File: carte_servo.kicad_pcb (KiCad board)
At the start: 4 copper layers, 48.4 x 99.2 mm, 157 parts, among them J1 Conn_01x04_Pin, J10 Conn_01x03_Male, J11 Transistor_2, J12 Transistor_1, J13 Transistor_4, J14 Transistor_.3, J16 Conn_01x04_Male, J17 Conn_01x04_Male, J18 Conn_01x03_Male, J19 Conn_01x03_Male, J2 Conn_02x04_Top_Bottom, J24 Conn_LEDs, J25 Conn_AX12, J29 Conn_AX12, J3 Conn_01x04_Pin, J5 Conn_01x03_Male, J6 Conn_01x03_Male, J7 Conn_01x03_Male, J8 Conn_01x03_Male, J9 Conn_01x03_Male, P1 USB_C_Plug_USB2.0, Q1 DMN2011UTS, Q2 DMN2011UTS, Q3 DMN2011UTS, Q4 DMN2011UTS, Q6 DMN2011UTS, Q7 CSD17307Q5A, Q8 CSD17579Q5A, SW2 SW_Push, U1 XGZP6897D_differential_pressu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, U10 TPS563200, U2 XGZP6897D_differential_pressu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, U3 TMC2208_SILENTSTEPSTICK, U4 TMC2208_SILENTSTEPSTICK, U5 74LVC2G241, U6 SN65HVD230, U7 LD1117S33TR_SOT223, U8 ESP32-S3-WROOM-1, U9 LM3150MH

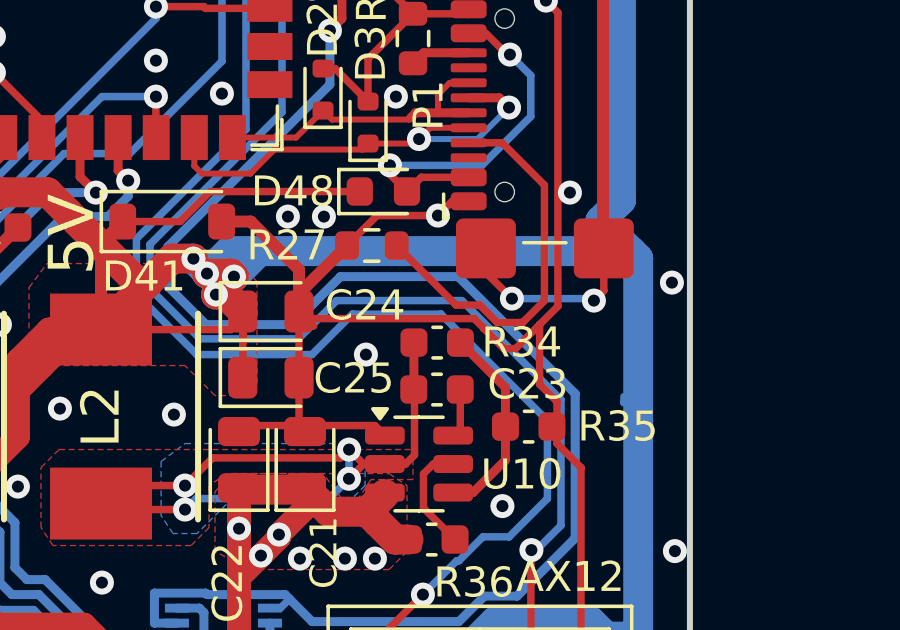
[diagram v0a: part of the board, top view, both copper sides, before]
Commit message: fix DCDC5V schematic
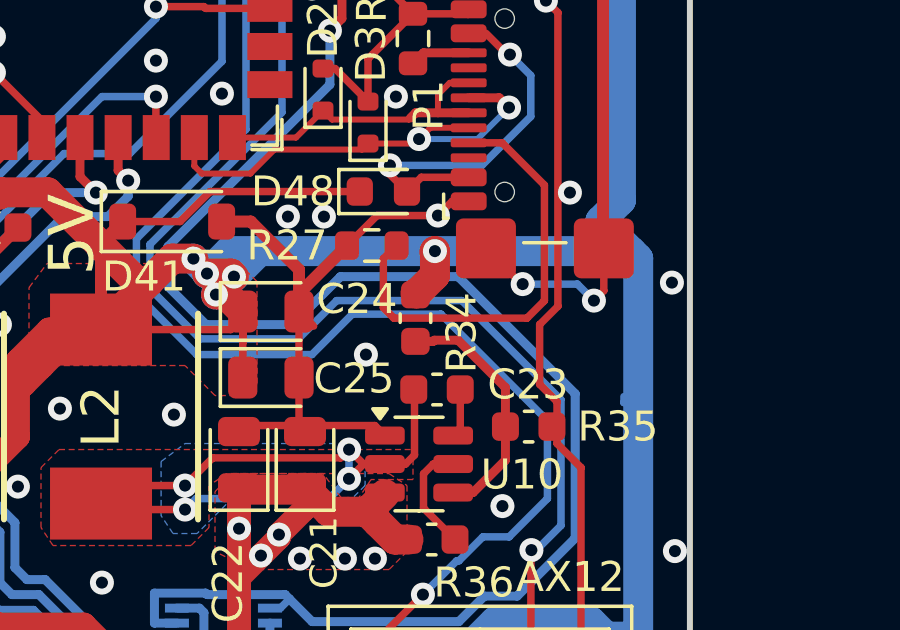
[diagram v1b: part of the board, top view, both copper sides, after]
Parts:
- L2: footprint Victor:INDPM6965X300N -> LibraryVictor:INDPM6965X300N
- moved R34 1.09 mm to (178.8, 115.0), turned to -90 degrees
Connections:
- R34 pad 1: /DCDC_5V/SW_DCDC5V -> 5V
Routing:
- net GND: track 601.5 -> 593.0 mm
- net 5V: track 338.2 -> 340.0 mm, vias 10 -> 11
- net Net-(P1-CC1): track 13.3 -> 15.0 mm
- net /DCDC_5V/SW_DCDC5V: track 26.1 -> 24.5 mm
- net Net-(U10-VFB): track 6.73 -> 8.28 mm

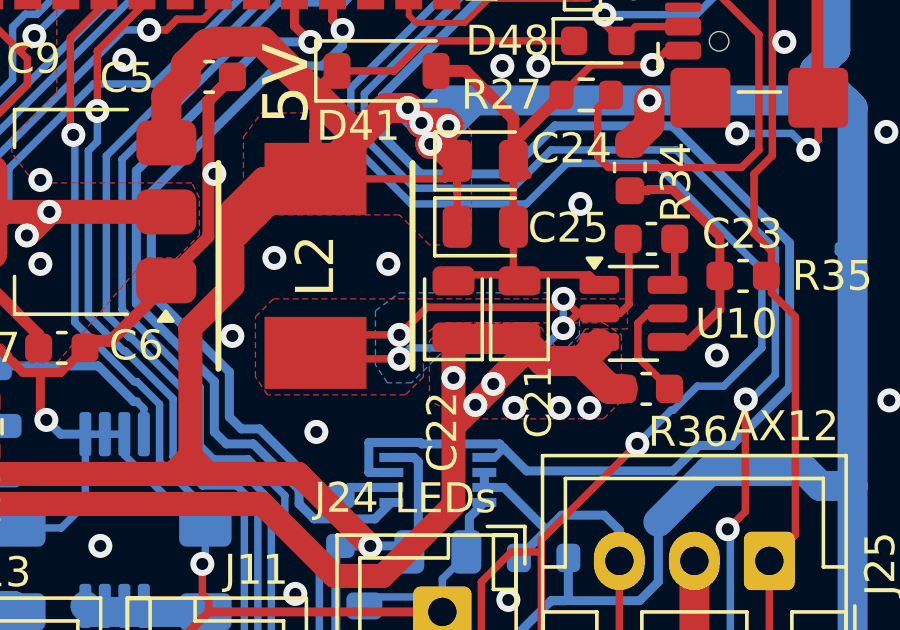
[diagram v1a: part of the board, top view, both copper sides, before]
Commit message: SW_5V is internal layer
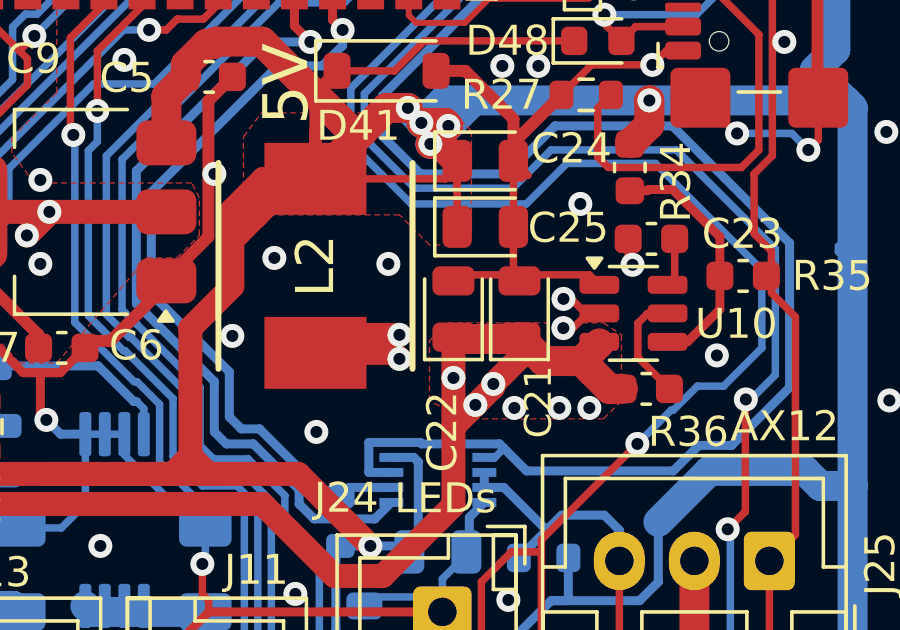
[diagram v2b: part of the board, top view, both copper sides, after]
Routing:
- net /DCDC_5V/SW_DCDC5V: track 24.5 -> 21.4 mm, vias 4 -> 5
- added copper zone on In2.Cu, net /DCDC_5V/SW_DCDC5V
- removed copper zone on B.Cu, net /DCDC_5V/SW_DCDC5V
- removed copper zone on F.Cu, net /DCDC_5V/SW_DCDC5V
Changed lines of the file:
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@@
 	)
 	(segment
-		(start 176.637492 119.365548)
-		(end 176.360944 119.642096)
-		(width 0.25)
-		(layer "F.Cu")
-		(net 104)
-	)
-	(segment
-		(start 172.092904 119.642096)
+		(start 176.895548 119.365548)
+		(end 176.637492 119.365548)
+		(width 0.25)
+		(layer "F.Cu")
+		(net 104)
+	)
+	(segment
+		(start 176.953157 120.338935)
+		(end 176.633515 120.338935)
+		(width 0.25)
+		(layer "F.Cu")
+		(net 104)
+	)
+	(segment
+		(start 178.795 118.085)
+		(end 178.94 118.23)
+		(width 0.25)
+		(layer "F.Cu")
+		(net 104)
+	)
+	(segment
+		(start 168.925 120.565)
 		(end 171.17 120.565)
-		(width 0.25)
-		(layer "F.Cu")
-		(net 104)
-	)
-	(segment
-		(start 171.17 121.365)
-		(end 168.77 121.365)
-		(width 0.25)
-		(layer "F.Cu")
-		(net 104)
-	)
-	(segment
-		(start 176.360944 119.642096)
-		(end 172.092904 119.642096)
-		(width 0.25)
-		(layer "F.Cu")
-		(net 104)
-	)
-	(segment
-		(start 176.637492 119.365548)
-		(end 177.119944 119.848)
-		(width 0.25)
-		(layer "F.Cu")
-		(net 104)
-	)
-	(segment
-		(start 177.119944 119.848)
-		(end 177.8325 119.848)
-		(width 0.25)
-		(layer "F.Cu")
-		(net 104)
-	)
-	(segment
-		(start 168.77 121.365)
-		(end 168.57 121.165)
+		(width 0.8)
+		(layer "F.Cu")
+		(net 104)
+	)
+	(segment
+		(start 168.37 121.12)
+		(end 168.925 120.565)
+		(width 0.8)
+		(layer "F.Cu")
+		(net 104)
+	)
+	(segment
+		(start 168.37 121.165)
+		(end 170.97 121.165)
+		(width 0.8)
+		(layer "F.Cu")
+		(net 104)
+	)
+	(segment
+		(start 177.444092 119.848)
+		(end 176.953157 120.338935)
 		(width 0.25)
 		(layer "F.Cu")
@@
 	)
 	(segment
-		(start 169.17 120.565)
-		(end 168.57 121.165)
+		(start 178.795 117.365)
+		(end 178.795 118.085)
 		(width 0.25)
 		(layer "F.Cu")
@@
 	)
 	(segment
-		(start 178.520908 119.848)
-		(end 178.82 119.548908)
-		(width 0.25)
-		(layer "F.Cu")
-		(net 104)
-	)
-	(segment
 		(start 177.8325 119.848)
-		(end 178.520908 119.848)
-		(width 0.25)
-		(layer "F.Cu")
-		(net 104)
-	)
-	(segment
-		(start 176.633515 120.338935)
-		(end 177.12445 119.848)
-		(width 0.25)
-		(layer "F.Cu")
-		(net 104)
-	)
-	(segment
-		(start 177.12445 119.848)
-		(end 177.8325 119.848)
-		(width 0.25)
-		(layer "F.Cu")
-		(net 104)
-	)
-	(segment
-		(start 178.82 119.548908)
-		(end 178.82 117.39)
-		(width 0.25)
-		(layer "F.Cu")
-		(net 104)
-	)
-	(segment
-		(start 171.17 120.565)
-		(end 169.17 120.565)
-		(width 0.25)
+		(end 177.444092 119.848)
+		(width 0.25)
+		(layer "F.Cu")
+		(net 104)
+	)
+	(segment
+		(start 177.378 119.848)
+		(end 176.895548 119.365548)
+		(width 0.25)
+		(layer "F.Cu")
+		(net 104)
+	)
+	(segment
+		(start 168.37 121.165)
+		(end 168.37 121.12)
+		(width 0.8)
+		(layer "F.Cu")
+		(net 104)
+	)
+	(segment
+		(start 177.8325 119.848)
+		(end 177.378 119.848)
+		(width 0.25)
+		(layer "F.Cu")
+		(net 104)
+	)
+	(segment
+		(start 170.97 121.165)
+		(end 171.17 121.365)
+		(width 0.8)
 		(layer "F.Cu")
 		(net 104)
@@
 	)
 	(via
+		(at 178.94 118.23)
+		(size 0.8)
+		(drill 0.4)
+		(layers "F.Cu" "B.Cu")
+		(net 104)
+	)
+	(via
 		(at 171.17 120.565)
 		(size 0.8)
@@
 	)
 	(segment
+		(start 176.633515 119.369525)
+		(end 176.637492 119.365548)
+		(width 0.25)
+		(layer "In2.Cu")
+		(net 104)
+	)
+	(segment
+		(start 177.05 119.79)
+		(end 171.945 119.79)
+		(width 0.25)
+		(layer "In2.Cu")
+		(net 104)
+	)
+	(segment
+		(start 171.17 120.565)
+		(end 171.17 121.365)
+		(width 0.25)
+		(layer "In2.Cu")
+		(net 104)
+	)
+	(segment
+		(start 176.637492 119.365548)
+		(end 176.637492 119.377492)
+		(width 0.25)
+		(layer "In2.Cu")
+		(net 104)
+	)
+	(segment
+		(start 176.637492 119.377492)
+		(end 177.05 119.79)
+		(width 0.25)
+		(layer "In2.Cu")
+		(net 104)
+	)
+	(segment
+		(start 178.29 119.8)
+		(end 178.94 119.15)
+		(width 0.25)
+		(layer "In2.Cu")
+		(net 104)
+	)
+	(segment
+		(start 171.945 119.79)
+		(end 171.17 120.565)
+		(width 0.25)
+		(layer "In2.Cu")
+		(net 104)
+	)
+	(segment
+		(start 178.94 119.15)
+		(end 178.94 118.23)
+		(width 0.25)
+		(layer "In2.Cu")
+		(net 104)
+	)
+	(segment
+		(start 177.05 119.79)
+		(end 178.28 119.79)
+		(width 0.25)
+		(layer "In2.Cu")
+		(net 104)
+	)
+	(segment
 		(start 176.633515 120.338935)
 		(end 176.633515 119.369525)
 		(width 0.25)
-		(layer "B.Cu")
-		(net 104)
-	)
-	(segment
-		(start 171.535 121)
-		(end 171.17 121.365)
-		(width 0.25)
-		(layer "B.Cu")
-		(net 104)
-	)
-	(segment
-		(start 175.97245 121)
-		(end 171.535 121)
-		(width 0.25)
-		(layer "B.Cu")
+		(layer "In2.Cu")
+		(net 104)
+	)
+	(segment
+		(start 178.28 119.79)
+		(end 178.29 119.8)
+		(width 0.25)
+		(layer "In2.Cu")
 		(net 104)
 	)
@@
 		(start 176.633515 119.369525)
 		(end 176.637492 119.365548)
-		(width 0.25)
-		(layer "B.Cu")
-		(net 104)
-	)
-	(segment
-		(start 176.633515 120.338935)
-		(end 175.97245 121)
 		(width 0.25)
 		(layer "B.Cu")
@@
 		(layer "F.Cu")
 		(net 115)
-	)
-	(zone
-		(net 104)
-		(net_name "/DCDC_5V/SW_DCDC5V")
-		(layer "F.Cu")
-		(hatch edge 0.5)
-		(priority 3)
-		(connect_pads yes
-			(clearance 0)
-		)
-		(min_thickness 0.25)
-		(filled_areas_thickness no)
-		(fill yes
-			(thermal_gap 0.5)
-			(thermal_bridge_width 0.5)
-		)
-		(polygon
-			(pts
-				(xy 166.37 119.965) (xy 166.97 119.365) (xy 173.37 119.365) (xy 178.77 119.365) (xy 178.77 120.365)
-				(xy 177.37 120.365) (xy 176.97 120.965) (xy 176.37 120.965) (xy 175.77 120.165) (xy 172.57 120.165)
-				(xy 171.97 120.565) (xy 171.97 121.965) (xy 171.37 122.565) (xy 166.77 122.565) (xy 166.37 121.965)
-			)
-		)
 	)
 	(zone
@@
 	)
 	(zone
+		(net 104)
+		(net_name "/DCDC_5V/SW_DCDC5V")
+		(layer "In2.Cu")
+		(hatch edge 0.5)
+		(priority 10)
+		(connect_pads
+			(clearance 0)
+		)
+		(min_thickness 0.25)
+		(filled_areas_thickness no)
+		(fill yes
+			(thermal_gap 0.5)
+			(thermal_bridge_width 0.5)
+		)
+		(polygon
+			(pts
+				(xy 169.88 121.42) (xy 169.9 119.94) (xy 171.11 118.9) (xy 177.41 118.9) (xy 177.81 119.38) (xy 177.79 120.34)
+				(xy 177.16 120.71) (xy 172.58 120.7) (xy 171.3 122.15) (xy 170.33 122.13) (xy 169.88 121.52)
+			)
+		)
+	)
+	(zone
 		(net 99)
 		(net_name "/ServoDCDC/SW")
@@
 			)
 		)
-	)
-	(zone
-		(net 104)
-		(net_name "/DCDC_5V/SW_DCDC5V")
-		(layer "B.Cu")
-		(hatch edge 0.5)
-		(priority 3)
-		(connect_pads yes
-			(clearance 0.508)
-		)
-		(min_thickness 0.25)
-		(filled_areas_thickness no)
-		(fill yes
-			(thermal_gap 0.5)
-			(thermal_bridge_width 0.5)
-		)
-		(polygon
-			(pts
-				(xy 170.37 121.565) (xy 170.37 119.765) (xy 171.17 119.165) (xy 176.57 119.165) (xy 177.17 119.765)
-				(xy 177.17 120.565) (xy 176.77 120.965) (xy 172.77 120.965) (xy 171.57 122.165) (xy 170.77 122.165)
-			)
-		)

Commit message: better routing
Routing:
- net 5V: track 340.0 -> 336.5 mm, vias 11 -> 7
- net Pressure_1: track 27.1 -> 29.1 mm
- net STEP_1: track 61.6 -> 63.2 mm, vias 0 -> 2
- net BATT_12V_elec: track 85.3 -> 86.8 mm, vias 13 -> 12
- net DIR_1: track 62.9 -> 63.9 mm, vias 0 -> 2
- net TRANSISTOR_1: track 28.8 -> 29.4 mm

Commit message: [WiP] add expander
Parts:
- removed D10, D9: D, Diode_SMD:D_SOD-882
- added C34: C_Small, Capacitor_SMD:C_0805_2012Metric, B.Cu at (147.8, 116.2)
- added C35: 100nF, Capacitor_SMD:C_0805_2012Metric, B.Cu at (139.6, 104.5)
- added J22: Conn_02x04_Top_Bottom, Connector_Molex:Molex_Micro-Fit_3.0_43045-0812_2x04_P3.00mm_Vertical, F.Cu at (136.2, 96.2)
- added J23: Conn_01x05, Connector_JST:JST_XH_B5B-XH-A_1x05_P2.50mm_Vertical, F.Cu at (137.2, 103.4)
- added J26: Conn_01x03, Connector_JST:JST_XH_B3B-XH-A_1x03_P2.50mm_Vertical, F.Cu at (135.8, 135.7)
- added J27: Conn_01x03, Connector_JST:JST_XH_B3B-XH-A_1x03_P2.50mm_Vertical, F.Cu at (135.8, 146.7)
- added J28: Conn_01x03, Connector_JST:JST_XH_B3B-XH-A_1x03_P2.50mm_Vertical, F.Cu at (135.8, 157.7)
- added J4: Conn_01x03, Connector_JST:JST_XH_B3B-XH-A_1x03_P2.50mm_Vertical, F.Cu at (135.8, 124.7)
- added R40: R_Small, Resistor_SMD:R_0603_1608Metric, B.Cu at (137.2, 128.2)
- added R41: R_Small, Resistor_SMD:R_0603_1608Metric, B.Cu at (137.2, 126.6)
- added R42: R_Small, Resistor_SMD:R_0603_1608Metric, B.Cu at (138.2, 133.6)
- added R43: R_Small, Resistor_SMD:R_0603_1608Metric, B.Cu at (138.6, 136.1)
- added R44: R_Small, Resistor_SMD:R_0603_1608Metric, B.Cu at (138.6, 143.2)
- added R45: R_Small, Resistor_SMD:R_0603_1608Metric, B.Cu at (138.6, 145.7)
- added R46: R_Small, Resistor_SMD:R_0603_1608Metric, B.Cu at (138.2, 154.2)
- added R47: R_Small, Resistor_SMD:R_0603_1608Metric, B.Cu at (138.0, 157.8)
- added U11: PCF8574ATS, Package_SO:SSOP-20_4.4x6.5mm_P0.65mm, B.Cu at (141.7, 117.9)
- J16, J17: value Conn_01x04_Male -> Conn_01x05; footprint Connector_PinHeader_2.54mm:PinHeader_1x04_P2.54mm_Vertical -> Connector_JST:JST_XH_B5B-XH-A_1x05_P2.50mm_Vertical
- L2: footprint LibraryVictor:INDPM6965X300N -> Victor:INDPM6965X300N
- moved D27 52.2 mm to (185.5, 75.8), turned to 0 degrees
- moved R3 51.8 mm to (184.4, 78.8)
- moved C1 10.8 mm to (154.7, 127.8), turned to 180 degrees
- moved H1 5.67 mm to (136.8, 65.3)
- moved D38 3.80 mm to (146.8, 108.8), turned to 90 degrees
- moved U1 3.44 mm to (146.3, 121.9), turned to 180 degrees
- moved J17 2.99 mm to (151.5, 103.4), turned to -90 degrees
- moved C28 1.78 mm to (149.4, 104.7), turned to 90 degrees
- moved D37 1.66 mm to (142.2, 105.2)
- moved J16 1.28 mm to (144.6, 103.4), turned to -90 degrees
- moved C29 1.20 mm to (146.8, 104.5), turned to 90 degrees
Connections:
- C28 pad 1: GND -> 5V
- C28 pad 2: 5V -> GND
- C29 pad 1: GND -> 5V
- C29 pad 2: 5V -> GND
- R38 pad 2: Net-(D9-A) -> /stepper_driver/PDN/UART
- R39 pad 1: Net-(D10-A) -> UartToStepper_2
- R39 pad 2: UartToStepper -> /stepper_driver1/PDN/UART
- U8 pad 7: TRANSISTOR_1 -> TRANSISTOR_4
- U8 pad 8: TRANSISTOR_4 -> UartToStepper_2
- U8 pad 9: TRANSISTOR_3 -> I2C_extra_0
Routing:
- net 5V: track 336.5 -> 393.3 mm, vias 7 -> 8
- net BATT_12V_elec: track 86.8 -> 133.2 mm, vias 12 -> 14
- net I2C_extra_0: track 0.00 -> 43.9 mm, vias 0 -> 2
- net GND: track 593.0 -> 549.2 mm, vias 137 -> 130
- net BATT_12V: track 319.2 -> 279.4 mm, vias 9 -> 11
- net /IO_expander/SIG_3: track 0.00 -> 39.5 mm
- net /IO_expander/SIG_2: track 0.00 -> 24.9 mm, vias 0 -> 1
- net SCL: track 61.8 -> 83.5 mm, vias 0 -> 1
- net TRANSISTOR_1: track 29.4 -> 10.6 mm, vias 1 -> 0
- net /IO_expander/SIG_0: track 0.00 -> 14.6 mm, vias 0 -> 1
- net I2C_extra_2: track 0.00 -> 14.4 mm
- net CAN-: track 44.5 -> 56.1 mm
- net /IO_expander/SIG_1: track 0.00 -> 11.3 mm, vias 0 -> 1
- net CAN+: track 41.8 -> 52.9 mm
- net UartToStepper: track 122.4 -> 113.8 mm, vias 4 -> 3
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- added copper zone on In1.Cu, net 12V_ELEC_P
- added copper zone on In1.Cu, net 12V_POW_P
- added copper zone on In1.Cu, net 24V_POW_P
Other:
- board size 48.4 x 99.2 mm -> 55.4 x 99.2 mm
- board text removed: "<= 12V on"

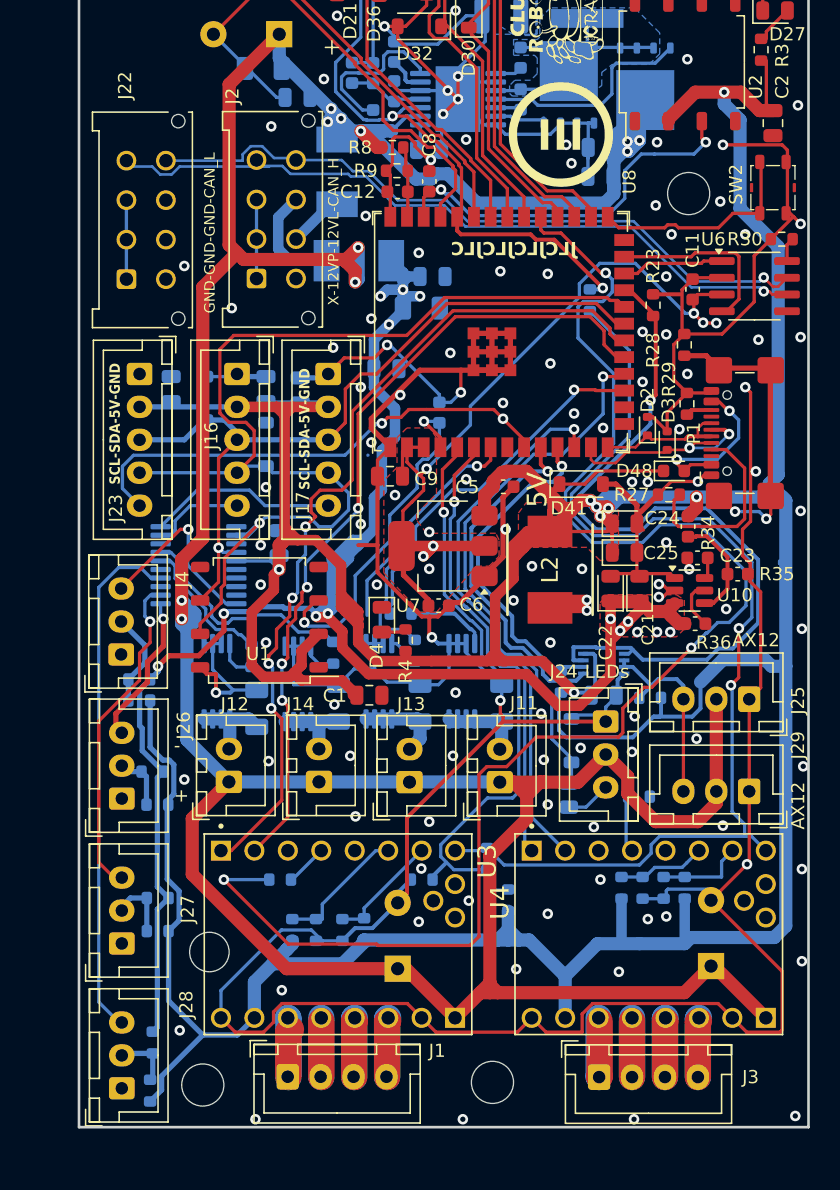
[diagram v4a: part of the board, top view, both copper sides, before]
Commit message: finish routing IO_exp + some fine-tuning
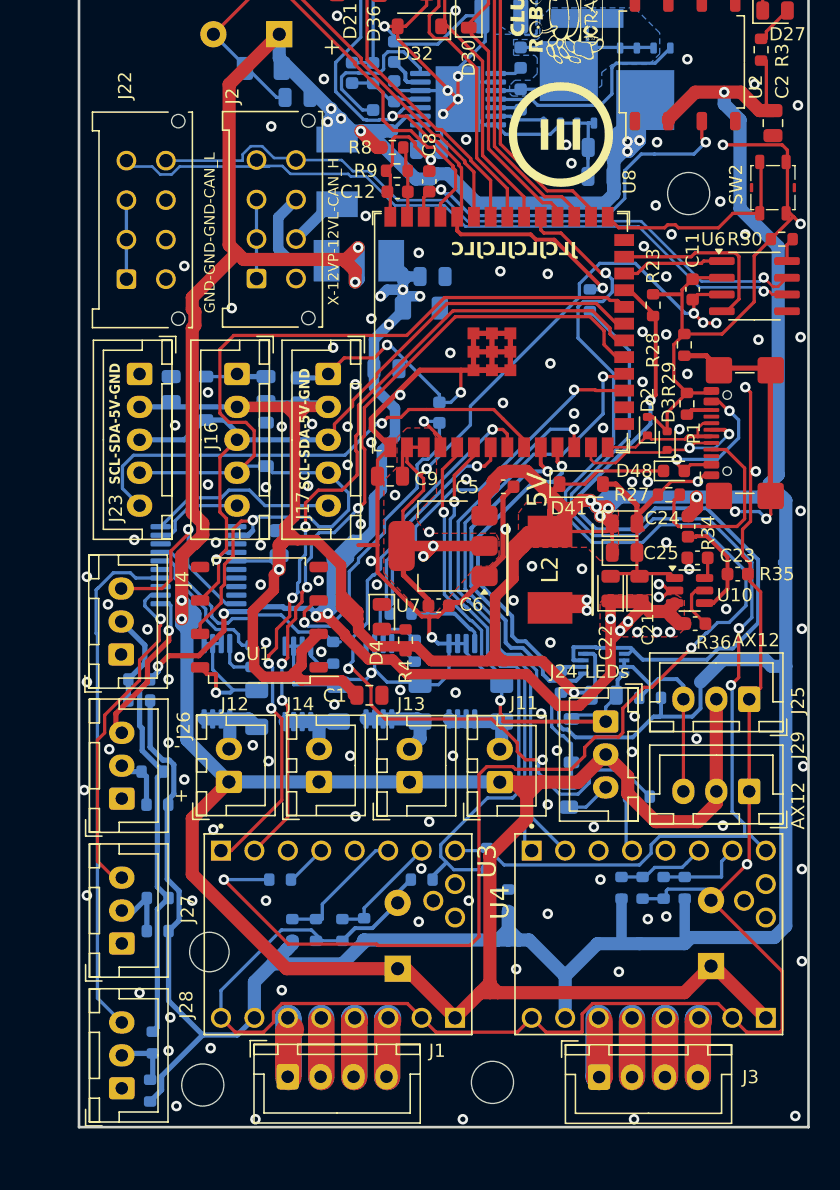
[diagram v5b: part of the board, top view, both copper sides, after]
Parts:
- moved D4 0.22 mm to (155.6, 121.8)
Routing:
- net UartToStepper_2: track 0.58 -> 56.8 mm, vias 0 -> 3
- net GND: track 549.2 -> 532.2 mm, vias 130 -> 163
- net I2C_extra_0: track 43.9 -> 37.3 mm, vias 2 -> 1
- net /IO_expander/SIG_0: track 14.6 -> 16.1 mm
- net SCL: track 83.5 -> 84.4 mm
- net /IO_expander/SIG_2: track 24.9 -> 25.8 mm
- net BATT_12V: track 279.4 -> 280.3 mm
- net /IO_expander/SIG_1: track 11.3 -> 12.2 mm
- net STEP_1: track 62.1 -> 63.0 mm
- net BATT_12V_elec: track 133.2 -> 132.5 mm
- net UartToStepper: track 113.8 -> 114.4 mm
